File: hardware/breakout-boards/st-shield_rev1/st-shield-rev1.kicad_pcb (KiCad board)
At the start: 4 copper layers, 63.5 x 50.8 mm, 201 parts, among them P1 CONN_01X06, P10 TST, P11 TST, P12 TST, P13 TST, P14 TST, P15 TST, P16 TST, P17 TST, P18 TST, P19 TST, P2 CONN_02X20, P20 TST, P21 TST, P22 TST, P23 TST, P24 TST, P25 TST, P26 TST, P27 TST, P28 TST, P3 CH_A, P4 CH_B, P5 CH_C, P6 PVDD, P7 GND, P8 TST, P9 TST, Q1 Q_PMOS_GSD, Q2 Q_PMOS_GSD, Q3 Q_NMOS_DGS, Q4 Q_NMOS_DGS, Q5 Q_NMOS_DGS, Q6 Q_NMOS_DGS, Q7 Q_NMOS_DGS, Q8 Q_NMOS_DGS, U1 DRV8301_DCA_56, U2 AD8691, U3 AD8691, U4 AD8691, U5 MCP9700-X_TT, U6 MCP9700-X_TT, U7 TLV62565DBVR, U8 AD8691

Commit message: st-shield-rev1: finished board layout. need to clean up (then send to fab)
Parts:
- removed C13, C14, C26, C29, C32: .1u, Capacitors_SMD:C_0603
- removed C15, C42: 100u, Capacitors_SMD:c_elec_6.3x7.7
- removed C16: 10u, Capacitors_SMD:C_2220
- removed C17: .015u, Capacitors_SMD:C_0603
- removed C25, C27, C30: .001u, Capacitors_SMD:C_0603
- removed C28, C31, C33: 100p, Capacitors_SMD:C_0603
- removed C44: 2.2u, Capacitors_SMD:C_0805
- removed C6: 120p, Capacitors_SMD:C_0603
- removed D5: D_Schottky_Small, DO-214AA(SMB):DO-214AA(SMB)
- removed D7: 3.3 Vbkdn, Diodes_SMD:SOD-123
- removed D9: 5Vbkdn, Diodes_SMD:SOD-123
- removed JP1: JUMPER, Pin_Headers:Pin_Header_Straight_1x02
- removed L1: 22u, hackvia:SMD_inductor_5x4mm
- removed L2: 2.2u, hackvia:SMD_inductor_5x4mm
- removed P10, P12, P23, P27, P28: TST, Measurement_Points:Measurement_Point_Round-SMD-Pad_Small
- removed P3: CH_A, Pin_Headers:Pin_Header_Straight_1x01
- removed P4: CH_B, Pin_Headers:Pin_Header_Straight_1x01
- removed P5: CH_C, Pin_Headers:Pin_Header_Straight_1x01
- removed P6: PVDD, Pin_Headers:Pin_Header_Straight_1x01
- removed P7: GND, Pin_Headers:Pin_Header_Straight_1x01
- removed R10: 220k, Resistors_SMD:R_0603
- removed R40: .0003, hackvia:WSL3921
- removed R41, R42, R46, R47, R50, R51: 1k, Resistors_SMD:R_0603
- removed R43, R44, R48, R49, R53, R54: 20k, Resistors_SMD:R_0603
- removed R45, R52, R55: 1.62k, Resistors_SMD:R_0603
- removed R68: 274k, Resistors_SMD:R_0603
- removed R69: 60.4k, Resistors_SMD:R_0603
- removed R7: 118k, Resistors_SMD:R_0603
- removed R71, R72: 82.5k, Resistors_SMD:R_0603
- removed R73: 100, Resistors_SMD:R_0603
- removed R8: 22.1k, Resistors_SMD:R_0603
- removed R9: 16.2k, Resistors_SMD:R_0603
- removed REF** (x23): hack-via, hackvia:hack-via
- removed U1: DRV8301_DCA_56, drv8301:-DCA56_6P35X3P61-M
- removed U2, U3, U4, U8: AD8691, ad8691:-KS_5
- removed U5, U6: MCP9700-X_TT, mcp9700:-SOT-23_MC
- removed U7: TLV62565DBVR, tlv62566:-DBV0005A
- removed W5, W6: NET-TIE, hackvia:nettie
- added MA: hack-via, hackvia:hack-via, F.Cu at (169.9, 116.0)
- added MB: hack-via, hackvia:hack-via, F.Cu at (153.4, 116.1)
- added MC: hack-via, hackvia:hack-via, F.Cu at (136.0, 116.0)
- added U11: DRV8303_DCA_48_SINGLE, DRV8303:drv8303-DCA48_4P42X3P48-M, F.Cu at (151.9, 85.8)
- added V1: hack-via, hackvia:hack-via, F.Cu at (179.6, 102.3)
- added V111111111: hack-via, hackvia:hack-via, F.Cu at (143.8, 81.4)
- added V111111111: hack-via, hackvia:hack-via, F.Cu at (123.8, 78.6)
- added V111111111: hack-via, hackvia:hack-via, F.Cu at (145.3, 78.5)
- added V111111111: hack-via, hackvia:hack-via, F.Cu at (180.8, 122.0)
- added V111111111: hack-via, hackvia:hack-via, F.Cu at (162.1, 119.9)
- added V111111111: hack-via, hackvia:hack-via, F.Cu at (159.9, 121.7)
- added V111111111: hack-via, hackvia:hack-via, F.Cu at (129.5, 120.5)
- added V111111111: hack-via, hackvia:hack-via, F.Cu at (143.3, 116.2)
- added V111111111: hack-via, hackvia:hack-via, F.Cu at (143.3, 117.1)
- added V111111111: hack-via, hackvia:hack-via, F.Cu at (126.5, 110.2)
- added V111111111: hack-via, hackvia:hack-via, F.Cu at (126.1, 109.6)
- added V111111111: hack-via, hackvia:hack-via, F.Cu at (143.8, 82.3)
- added V111111111: hack-via, hackvia:hack-via, F.Cu at (129.3, 116.3)
- added V111111111: hack-via, hackvia:hack-via, F.Cu at (124.7, 117.1)
- added V111111111: hack-via, hackvia:hack-via, F.Cu at (153.5, 75.2)
- added V111111111: hack-via, hackvia:hack-via, F.Cu at (143.8, 77.9)
- added V111111111: hack-via, hackvia:hack-via, F.Cu at (137.2, 76.2)
- added V111111111: hack-via, hackvia:hack-via, F.Cu at (139.7, 76.2)
- added V111111111: hack-via, hackvia:hack-via, F.Cu at (160.4, 95.5)
- added V111111111: hack-via, hackvia:hack-via, F.Cu at (165.9, 95.6)
- added V111111111: hack-via, hackvia:hack-via, F.Cu at (165.9, 92.2)
- added V111111111: hack-via, hackvia:hack-via, F.Cu at (160.5, 92.2)
- added V111111111: hack-via, hackvia:hack-via, F.Cu at (145.3, 82.3)
- added V111111111: hack-via, hackvia:hack-via, F.Cu at (120.9, 97.0)
- added V111111111: hack-via, hackvia:hack-via, F.Cu at (121.0, 104.6)
- added V111111111: hack-via, hackvia:hack-via, F.Cu at (122.3, 114.9)
- added V111111111: hack-via, hackvia:hack-via, F.Cu at (124.8, 122.2)
- added V111111111: hack-via, hackvia:hack-via, F.Cu at (120.9, 118.0)
- added V111111111: hack-via, hackvia:hack-via, F.Cu at (120.9, 122.2)
- added V111111111: hack-via, hackvia:hack-via, F.Cu at (124.8, 69.5)
- added V111111111: hack-via, hackvia:hack-via, F.Cu at (122.8, 69.5)
- added V111111111: hack-via, hackvia:hack-via, F.Cu at (120.5, 69.5)
- added V111111111: hack-via, hackvia:hack-via, F.Cu at (126.6, 80.9)
- added V111111111: hack-via, hackvia:hack-via, F.Cu at (145.3, 81.4)
- added V111111111: hack-via, hackvia:hack-via, F.Cu at (124.1, 83.4)
- added V111111111: hack-via, hackvia:hack-via, F.Cu at (127.6, 88.5)
- added V111111111: hack-via, hackvia:hack-via, F.Cu at (129.0, 88.6)
- added V111111111: hack-via, hackvia:hack-via, F.Cu at (131.6, 92.7)
- added V111111111: hack-via, hackvia:hack-via, F.Cu at (130.2, 95.5)
- added V111111111: hack-via, hackvia:hack-via, F.Cu at (131.1, 95.5)
- added V111111111: hack-via, hackvia:hack-via, F.Cu at (150.1, 84.5)
- added V111111111: hack-via, hackvia:hack-via, F.Cu at (140.0, 81.4)
- added V111111111: hack-via, hackvia:hack-via, F.Cu at (140.3, 82.2)
- added V111111111: hack-via, hackvia:hack-via, F.Cu at (140.3, 83.1)
- added V111111111: hack-via, hackvia:hack-via, F.Cu at (141.4, 83.1)
- added V111111111: hack-via, hackvia:hack-via, F.Cu at (162.1, 117.5)
- added V111111111111: hack-via, hackvia:hack-via, F.Cu at (131.6, 112.9)
- added V1111111111111: hack-via, hackvia:hack-via, F.Cu at (148.8, 112.9)
- added V11111111111111: hack-via, hackvia:hack-via, F.Cu at (165.4, 112.9)
- added V1111111111111111: hack-via, hackvia:hack-via, F.Cu at (175.1, 81.8)
- added V1111111111111112: hack-via, hackvia:hack-via, F.Cu at (175.1, 83.3)
- added V1111111111111113: hack-via, hackvia:hack-via, F.Cu at (175.1, 84.8)
- added V1111111111111114: hack-via, hackvia:hack-via, F.Cu at (175.1, 86.4)
- added V1111111111111115: hack-via, hackvia:hack-via, F.Cu at (175.1, 87.9)
- added V1111111111111116: hack-via, hackvia:hack-via, F.Cu at (175.1, 89.4)
- added V1111111111111121: hack-via, hackvia:hack-via, F.Cu at (176.4, 81.8)
- added V1111111111111122: hack-via, hackvia:hack-via, F.Cu at (176.4, 83.3)
- added V1111111111111123: hack-via, hackvia:hack-via, F.Cu at (176.4, 84.8)
- added V1111111111111124: hack-via, hackvia:hack-via, F.Cu at (176.4, 86.4)
- added V1111111111111125: hack-via, hackvia:hack-via, F.Cu at (176.4, 87.9)
- added V1111111111111126: hack-via, hackvia:hack-via, F.Cu at (176.4, 89.4)
- added V1111111111111131: hack-via, hackvia:hack-via, F.Cu at (177.7, 81.8)
- added V1111111111111132: hack-via, hackvia:hack-via, F.Cu at (177.7, 83.3)
- added V1111111111111133: hack-via, hackvia:hack-via, F.Cu at (177.7, 84.8)
- added V1111111111111134: hack-via, hackvia:hack-via, F.Cu at (177.7, 86.4)
- added V1111111111111135: hack-via, hackvia:hack-via, F.Cu at (177.7, 87.9)
- added V1111111111111136: hack-via, hackvia:hack-via, F.Cu at (177.7, 89.4)
- added V1111111111111141: hack-via, hackvia:hack-via, F.Cu at (178.9, 81.8)
- added V1111111111111142: hack-via, hackvia:hack-via, F.Cu at (178.9, 83.3)
- added V1111111111111143: hack-via, hackvia:hack-via, F.Cu at (178.9, 84.8)
- added V1111111111111144: hack-via, hackvia:hack-via, F.Cu at (178.9, 86.4)
- added V1111111111111145: hack-via, hackvia:hack-via, F.Cu at (178.9, 87.9)
- added V1111111111111146: hack-via, hackvia:hack-via, F.Cu at (178.9, 89.4)
- added V1111111111111151: hack-via, hackvia:hack-via, F.Cu at (180.2, 81.8)
- added V1111111111111152: hack-via, hackvia:hack-via, F.Cu at (180.2, 83.3)
- added V1111111111111153: hack-via, hackvia:hack-via, F.Cu at (180.2, 84.8)
- added V1111111111111154: hack-via, hackvia:hack-via, F.Cu at (180.2, 86.4)
- added V1111111111111155: hack-via, hackvia:hack-via, F.Cu at (180.2, 87.9)
- added V1111111111111156: hack-via, hackvia:hack-via, F.Cu at (180.2, 89.4)
- added V1111111111111161: hack-via, hackvia:hack-via, F.Cu at (181.5, 81.8)
- added V1111111111111162: hack-via, hackvia:hack-via, F.Cu at (181.5, 83.3)
- added V1111111111111163: hack-via, hackvia:hack-via, F.Cu at (181.5, 84.8)
- added V1111111111111164: hack-via, hackvia:hack-via, F.Cu at (181.5, 86.4)
- added V1111111111111165: hack-via, hackvia:hack-via, F.Cu at (181.5, 87.9)
- added V1111111111111166: hack-via, hackvia:hack-via, F.Cu at (181.5, 89.4)
- added V11111111111112: hack-via, hackvia:hack-via, F.Cu at (165.4, 114.2)
- added V11111111111113: hack-via, hackvia:hack-via, F.Cu at (165.4, 115.4)
- added V11111111111114: hack-via, hackvia:hack-via, F.Cu at (165.4, 116.7)
- added V11111111111115: hack-via, hackvia:hack-via, F.Cu at (165.4, 118.0)
- added V11111111111116: hack-via, hackvia:hack-via, F.Cu at (165.4, 119.3)
- added V1111111111112: hack-via, hackvia:hack-via, F.Cu at (148.8, 114.2)
- added V11111111111121: hack-via, hackvia:hack-via, F.Cu at (166.9, 112.9)
- added V11111111111122: hack-via, hackvia:hack-via, F.Cu at (166.9, 114.2)
- added V11111111111123: hack-via, hackvia:hack-via, F.Cu at (166.9, 115.4)
- added V11111111111124: hack-via, hackvia:hack-via, F.Cu at (166.9, 116.7)
- added V11111111111125: hack-via, hackvia:hack-via, F.Cu at (166.9, 118.0)
- added V11111111111126: hack-via, hackvia:hack-via, F.Cu at (166.9, 119.3)
- added V1111111111113: hack-via, hackvia:hack-via, F.Cu at (148.8, 115.4)
- added V11111111111131: hack-via, hackvia:hack-via, F.Cu at (168.4, 112.9)
- added V11111111111132: hack-via, hackvia:hack-via, F.Cu at (168.4, 114.2)
- added V11111111111133: hack-via, hackvia:hack-via, F.Cu at (168.4, 115.4)
- added V11111111111134: hack-via, hackvia:hack-via, F.Cu at (168.4, 116.7)
- added V11111111111135: hack-via, hackvia:hack-via, F.Cu at (168.4, 118.0)
- added V11111111111136: hack-via, hackvia:hack-via, F.Cu at (168.4, 119.3)
- added V1111111111114: hack-via, hackvia:hack-via, F.Cu at (148.8, 116.7)
- added V11111111111141: hack-via, hackvia:hack-via, F.Cu at (169.9, 112.9)
- added V11111111111142: hack-via, hackvia:hack-via, F.Cu at (169.9, 114.2)
- added V11111111111143: hack-via, hackvia:hack-via, F.Cu at (169.9, 115.4)
- added V11111111111144: hack-via, hackvia:hack-via, F.Cu at (169.9, 116.7)
- added V11111111111145: hack-via, hackvia:hack-via, F.Cu at (169.9, 118.0)
- added V11111111111146: hack-via, hackvia:hack-via, F.Cu at (169.9, 119.3)
- added V1111111111115: hack-via, hackvia:hack-via, F.Cu at (148.8, 118.0)
- added V11111111111151: hack-via, hackvia:hack-via, F.Cu at (171.4, 112.9)
- added V11111111111152: hack-via, hackvia:hack-via, F.Cu at (171.4, 114.2)
- added V11111111111153: hack-via, hackvia:hack-via, F.Cu at (171.4, 115.4)
- added V11111111111154: hack-via, hackvia:hack-via, F.Cu at (171.4, 116.7)
- added V11111111111155: hack-via, hackvia:hack-via, F.Cu at (171.4, 118.0)
- added V11111111111156: hack-via, hackvia:hack-via, F.Cu at (171.4, 119.3)
- added V1111111111116: hack-via, hackvia:hack-via, F.Cu at (148.8, 119.3)
- added V11111111111161: hack-via, hackvia:hack-via, F.Cu at (173.0, 112.9)
- added V11111111111162: hack-via, hackvia:hack-via, F.Cu at (173.0, 114.2)
- added V11111111111163: hack-via, hackvia:hack-via, F.Cu at (173.0, 115.4)
- added V11111111111164: hack-via, hackvia:hack-via, F.Cu at (173.0, 116.7)
- added V11111111111165: hack-via, hackvia:hack-via, F.Cu at (173.0, 118.0)
- added V11111111111166: hack-via, hackvia:hack-via, F.Cu at (173.0, 119.3)
- added V11111111111171: hack-via, hackvia:hack-via, F.Cu at (174.5, 112.9)
- added V11111111111172: hack-via, hackvia:hack-via, F.Cu at (174.5, 114.2)
- added V11111111111173: hack-via, hackvia:hack-via, F.Cu at (174.5, 115.4)
- added V11111111111174: hack-via, hackvia:hack-via, F.Cu at (174.5, 116.7)
- added V11111111111175: hack-via, hackvia:hack-via, F.Cu at (174.5, 118.0)
- added V11111111111176: hack-via, hackvia:hack-via, F.Cu at (174.5, 119.3)
- added V111111111112: hack-via, hackvia:hack-via, F.Cu at (131.6, 114.2)
- added V1111111111121: hack-via, hackvia:hack-via, F.Cu at (150.4, 112.9)
- added V1111111111122: hack-via, hackvia:hack-via, F.Cu at (150.4, 114.2)
- added V1111111111123: hack-via, hackvia:hack-via, F.Cu at (150.4, 115.4)
- added V1111111111124: hack-via, hackvia:hack-via, F.Cu at (150.4, 116.7)
- added V1111111111125: hack-via, hackvia:hack-via, F.Cu at (150.4, 118.0)
- added V1111111111126: hack-via, hackvia:hack-via, F.Cu at (150.4, 119.3)
- added V111111111113: hack-via, hackvia:hack-via, F.Cu at (131.6, 115.4)
- added V1111111111131: hack-via, hackvia:hack-via, F.Cu at (151.9, 112.9)
- added V1111111111132: hack-via, hackvia:hack-via, F.Cu at (151.9, 114.2)
- added V1111111111133: hack-via, hackvia:hack-via, F.Cu at (151.9, 115.4)
- added V1111111111134: hack-via, hackvia:hack-via, F.Cu at (151.9, 116.7)
- added V1111111111135: hack-via, hackvia:hack-via, F.Cu at (151.9, 118.0)
- added V1111111111136: hack-via, hackvia:hack-via, F.Cu at (151.9, 119.3)
- added V111111111114: hack-via, hackvia:hack-via, F.Cu at (131.6, 116.7)
- added V1111111111141: hack-via, hackvia:hack-via, F.Cu at (153.4, 112.9)
- added V1111111111142: hack-via, hackvia:hack-via, F.Cu at (153.4, 114.2)
- added V1111111111143: hack-via, hackvia:hack-via, F.Cu at (153.4, 115.4)
- added V1111111111144: hack-via, hackvia:hack-via, F.Cu at (153.4, 116.7)
- added V1111111111145: hack-via, hackvia:hack-via, F.Cu at (153.4, 118.0)
- added V1111111111146: hack-via, hackvia:hack-via, F.Cu at (153.4, 119.3)
- added V111111111115: hack-via, hackvia:hack-via, F.Cu at (131.6, 118.0)
- added V1111111111151: hack-via, hackvia:hack-via, F.Cu at (154.9, 112.9)
- added V1111111111152: hack-via, hackvia:hack-via, F.Cu at (154.9, 114.2)
- added V1111111111153: hack-via, hackvia:hack-via, F.Cu at (154.9, 115.4)
- added V1111111111154: hack-via, hackvia:hack-via, F.Cu at (154.9, 116.7)
- added V1111111111155: hack-via, hackvia:hack-via, F.Cu at (154.9, 118.0)
- added V1111111111156: hack-via, hackvia:hack-via, F.Cu at (154.9, 119.3)
- added V111111111116: hack-via, hackvia:hack-via, F.Cu at (131.6, 119.3)
- added V1111111111161: hack-via, hackvia:hack-via, F.Cu at (156.5, 112.9)
- added V1111111111162: hack-via, hackvia:hack-via, F.Cu at (156.5, 114.2)
- added V1111111111163: hack-via, hackvia:hack-via, F.Cu at (156.5, 115.4)
- added V1111111111164: hack-via, hackvia:hack-via, F.Cu at (156.5, 116.7)
- added V1111111111165: hack-via, hackvia:hack-via, F.Cu at (156.5, 118.0)
- added V1111111111166: hack-via, hackvia:hack-via, F.Cu at (156.5, 119.3)
- added V1111111111171: hack-via, hackvia:hack-via, F.Cu at (158.0, 112.9)
- added V1111111111172: hack-via, hackvia:hack-via, F.Cu at (158.0, 114.2)
- added V1111111111173: hack-via, hackvia:hack-via, F.Cu at (158.0, 115.4)
- added V1111111111174: hack-via, hackvia:hack-via, F.Cu at (158.0, 116.7)
- added V1111111111175: hack-via, hackvia:hack-via, F.Cu at (158.0, 118.0)
- added V1111111111176: hack-via, hackvia:hack-via, F.Cu at (158.0, 119.3)
- added V111111111121: hack-via, hackvia:hack-via, F.Cu at (133.1, 112.9)
- added V111111111122: hack-via, hackvia:hack-via, F.Cu at (133.1, 114.2)
- added V111111111123: hack-via, hackvia:hack-via, F.Cu at (133.1, 115.4)
- added V111111111124: hack-via, hackvia:hack-via, F.Cu at (133.1, 116.7)
- added V111111111125: hack-via, hackvia:hack-via, F.Cu at (133.1, 118.0)
- added V111111111126: hack-via, hackvia:hack-via, F.Cu at (133.1, 119.3)
- added V111111111131: hack-via, hackvia:hack-via, F.Cu at (134.6, 112.9)
- added V111111111132: hack-via, hackvia:hack-via, F.Cu at (134.6, 114.2)
- added V111111111133: hack-via, hackvia:hack-via, F.Cu at (134.6, 115.4)
- added V111111111134: hack-via, hackvia:hack-via, F.Cu at (134.6, 116.7)
- added V111111111135: hack-via, hackvia:hack-via, F.Cu at (134.6, 118.0)
- added V111111111136: hack-via, hackvia:hack-via, F.Cu at (134.6, 119.3)
- added V111111111141: hack-via, hackvia:hack-via, F.Cu at (136.1, 112.9)
- added V111111111142: hack-via, hackvia:hack-via, F.Cu at (136.1, 114.2)
- added V111111111143: hack-via, hackvia:hack-via, F.Cu at (136.1, 115.4)
- added V111111111144: hack-via, hackvia:hack-via, F.Cu at (136.1, 116.7)
- added V111111111145: hack-via, hackvia:hack-via, F.Cu at (136.1, 118.0)
- added V111111111146: hack-via, hackvia:hack-via, F.Cu at (136.1, 119.3)
- added V111111111151: hack-via, hackvia:hack-via, F.Cu at (137.7, 112.9)
- added V111111111152: hack-via, hackvia:hack-via, F.Cu at (137.7, 114.2)
- added V111111111153: hack-via, hackvia:hack-via, F.Cu at (137.7, 115.4)
- added V111111111154: hack-via, hackvia:hack-via, F.Cu at (137.7, 116.7)
- added V111111111155: hack-via, hackvia:hack-via, F.Cu at (137.7, 118.0)
- added V111111111156: hack-via, hackvia:hack-via, F.Cu at (137.7, 119.3)
- added V111111111161: hack-via, hackvia:hack-via, F.Cu at (139.2, 112.9)
- added V111111111162: hack-via, hackvia:hack-via, F.Cu at (139.2, 114.2)
- added V111111111163: hack-via, hackvia:hack-via, F.Cu at (139.2, 115.4)
- added V111111111164: hack-via, hackvia:hack-via, F.Cu at (139.2, 116.7)
- added V111111111165: hack-via, hackvia:hack-via, F.Cu at (139.2, 118.0)
- added V111111111166: hack-via, hackvia:hack-via, F.Cu at (139.2, 119.3)
- added V111111111171: hack-via, hackvia:hack-via, F.Cu at (140.7, 112.9)
- added V111111111172: hack-via, hackvia:hack-via, F.Cu at (140.7, 114.2)
- added V111111111173: hack-via, hackvia:hack-via, F.Cu at (140.7, 115.4)
- added V111111111174: hack-via, hackvia:hack-via, F.Cu at (140.7, 116.7)
- added V111111111175: hack-via, hackvia:hack-via, F.Cu at (140.7, 118.0)
- added V111111111176: hack-via, hackvia:hack-via, F.Cu at (140.7, 119.3)
- added V111111112: hack-via, hackvia:hack-via, F.Cu at (150.1, 85.1)
- added V111111113: hack-via, hackvia:hack-via, F.Cu at (150.1, 85.7)
- added V111111114: hack-via, hackvia:hack-via, F.Cu at (150.1, 86.4)
- added V111111115: hack-via, hackvia:hack-via, F.Cu at (150.1, 87.0)
- added V111111121: hack-via, hackvia:hack-via, F.Cu at (151.0, 84.5)
- added V111111122: hack-via, hackvia:hack-via, F.Cu at (151.0, 85.1)
- added V111111123: hack-via, hackvia:hack-via, F.Cu at (151.0, 85.7)
- added V111111124: hack-via, hackvia:hack-via, F.Cu at (151.0, 86.4)
- added V111111125: hack-via, hackvia:hack-via, F.Cu at (151.0, 87.0)
- added V111111131: hack-via, hackvia:hack-via, F.Cu at (151.9, 84.5)
- added V111111132: hack-via, hackvia:hack-via, F.Cu at (151.9, 85.1)
- added V111111133: hack-via, hackvia:hack-via, F.Cu at (151.9, 85.7)
- added V111111134: hack-via, hackvia:hack-via, F.Cu at (151.9, 86.4)
- added V111111135: hack-via, hackvia:hack-via, F.Cu at (151.9, 87.0)
- added V111111141: hack-via, hackvia:hack-via, F.Cu at (152.8, 84.5)
- added V111111142: hack-via, hackvia:hack-via, F.Cu at (152.8, 85.1)
- added V111111143: hack-via, hackvia:hack-via, F.Cu at (152.8, 85.7)
- added V111111144: hack-via, hackvia:hack-via, F.Cu at (152.8, 86.4)
- added V111111145: hack-via, hackvia:hack-via, F.Cu at (152.8, 87.0)
- added V111111151: hack-via, hackvia:hack-via, F.Cu at (153.7, 84.5)
- added V111111152: hack-via, hackvia:hack-via, F.Cu at (153.7, 85.1)
- added V111111153: hack-via, hackvia:hack-via, F.Cu at (153.7, 85.7)
- added V111111154: hack-via, hackvia:hack-via, F.Cu at (153.7, 86.4)
- added V111111155: hack-via, hackvia:hack-via, F.Cu at (153.7, 87.0)
- added V2: hack-via, hackvia:hack-via, F.Cu at (126.2, 101.7)
- added V3: hack-via, hackvia:hack-via, F.Cu at (134.5, 85.3)
- added V4: hack-via, hackvia:hack-via, F.Cu at (178.2, 85.4)
- C18, C20, C21, C23, R14, R15, R19, R20, R21, R23, R24, R31, R34, R35, R39: moved to B.Cu
- C4: value .1u -> 1000p; moved to B.Cu
- C5: value 6800p -> 1000p; moved to B.Cu
- C9: value 10u -> 4.7u
- R1, R2, R3, R4: footprint Resistors_SMD:R_0805 -> Resistors_SMD:R_0603
- moved R59 251.9 mm to (124.2, 91.3), turned to 270 degrees
- moved R60 251.3 mm to (124.2, 94.2), turned to 270 degrees
- moved R58 247.5 mm to (124.2, 88.5), turned to 270 degrees
- moved R61 245.9 mm to (126.4, 88.5), turned to 270 degrees
- moved R63 241.0 mm to (126.4, 94.2), turned to 270 degrees
- moved C36 240.2 mm to (128.3, 91.6), turned to 270 degrees
- moved R62 237.0 mm to (126.4, 91.3), turned to 270 degrees
- moved C35 235.6 mm to (128.3, 88.5), turned to 270 degrees
- moved C37 229.7 mm to (128.3, 94.7), turned to 270 degrees
- moved P26 227.8 mm to (130.5, 94.0)
- moved R65 224.4 mm to (130.8, 81.0)
- moved R66 221.8 mm to (137.9, 82.4), turned to 180 degrees
- moved P24 221.5 mm to (130.5, 88.8)
- moved P25 221.1 mm to (130.4, 91.6)
- moved R64 211.8 mm to (138.0, 88.0), turned to 270 degrees
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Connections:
- C4 pad 1: 3V3 -> /MOSFET Array/CUR_CP
- C4 pad 2: GND -> /MOSFET Array/CUR_CN
- C5 pad 1: Net-(C5-Pad1) -> /MOSFET Array/CUR_BP
- C5 pad 2: GND -> /MOSFET Array/CUR_BN
- P2 pad 1: Net-(JP1-Pad2) -> 3V3
- P2 pad 16: /Temperature Sensors/T1 -> /FET Driver/SO1
- P2 pad 18: /Temperature Sensors/T2 -> /FET Driver/SO2
- P2 pad 20: Net-(P2-Pad20) -> (no net)
- P2 pad 22: /Shunt Amplifiers/IA -> /Hall Effect Sensor Filters/HALL_A_OUT
- P2 pad 24: /Shunt Amplifiers/IB -> /Hall Effect Sensor Filters/HALL_B_OUT
- P2 pad 26: /Shunt Amplifiers/IC -> (no net)
- P2 pad 28: /Hall Effect Sensor Filters/HALL_A_OUT -> /Power Management/DC_IN
- P2 pad 3: Net-(JP1-Pad2) -> 5V
- P2 pad 30: /Hall Effect Sensor Filters/HALL_B_OUT -> GND
- P2 pad 32: /Hall Effect Sensor Filters/HALL_C_OUT -> GND
- P2 pad 34: /Power Management/DC_IN -> GND
- P20 pad 1: Net-(P20-Pad1) -> (no net)
- Q4 pad 3: /FET Driver/SL_A -> GND
- R22 pad 2: /FET Driver/SL_A -> /FET Driver/SL_C
- W1 pad 1: /FET Driver/SL_A -> /FET Driver/SL_C
- W1 pad 2: /MOSFET Array/CUR_AP -> /MOSFET Array/CUR_CP
- W2 pad 2: /MOSFET Array/CUR_AN -> /MOSFET Array/CUR_CN
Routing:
- net /MOSFET Array/AEMF: track 0.00 -> 116.0 mm, vias 0 -> 2
- net 3V3: track 1.27 -> 115.2 mm, vias 0 -> 1
- net /MOSFET Array/BEMF: track 0.00 -> 100.6 mm, vias 0 -> 1
- net GND: track 1.50 -> 90.1 mm, vias 0 -> 2
- net /Hall Effect Sensor Filters/HALL_A_OUT: track 0.00 -> 77.6 mm, vias 0 -> 2
- net /MOSFET Array/MOTOR_N: track 0.00 -> 72.3 mm, vias 0 -> 4
- net /MOSFET Array/CEMF: track 0.00 -> 65.6 mm, vias 0 -> 1
- net Net-(R27-Pad1): track 0.00 -> 64.3 mm
- net /Power Management/DC_IN: track 0.00 -> 51.5 mm
- net /Hall Effect Sensor Filters/HALL_B_OUT: track 0.00 -> 47.1 mm, vias 0 -> 1
- net /Temperature Sensors/T0: track 0.00 -> 30.2 mm
- net /MOSFET Array/MOTOR_A: track 3.22 -> 32.1 mm, vias 0 -> 2
- net /MOSFET Array/A_HI: track 0.00 -> 27.5 mm, vias 0 -> 2
- net /FET Driver/SO2: track 0.00 -> 26.9 mm, vias 0 -> 1
- net /FET Driver/FAULT: track 0.00 -> 23.2 mm
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- added copper zone on F.Cu, net GND
- removed copper zone on B.Cu, net /FET Driver/SL_A
- removed copper zone on In2.Cu, net GND
- removed copper zone on In1.Cu, net PVDD
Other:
- board size 63.5 x 50.8 mm -> 63.5 x 55.4 mm
- copper layers 4 -> 2
- board text added: "A"
- board text added: "B"
- board text added: "C"
- board text added: "DEBUG"
- board text added: "FAULT"
- board text added: "G N D"
- board text added: "OCTW"
- board text added: "P V D D"
- board text added: "PWR"

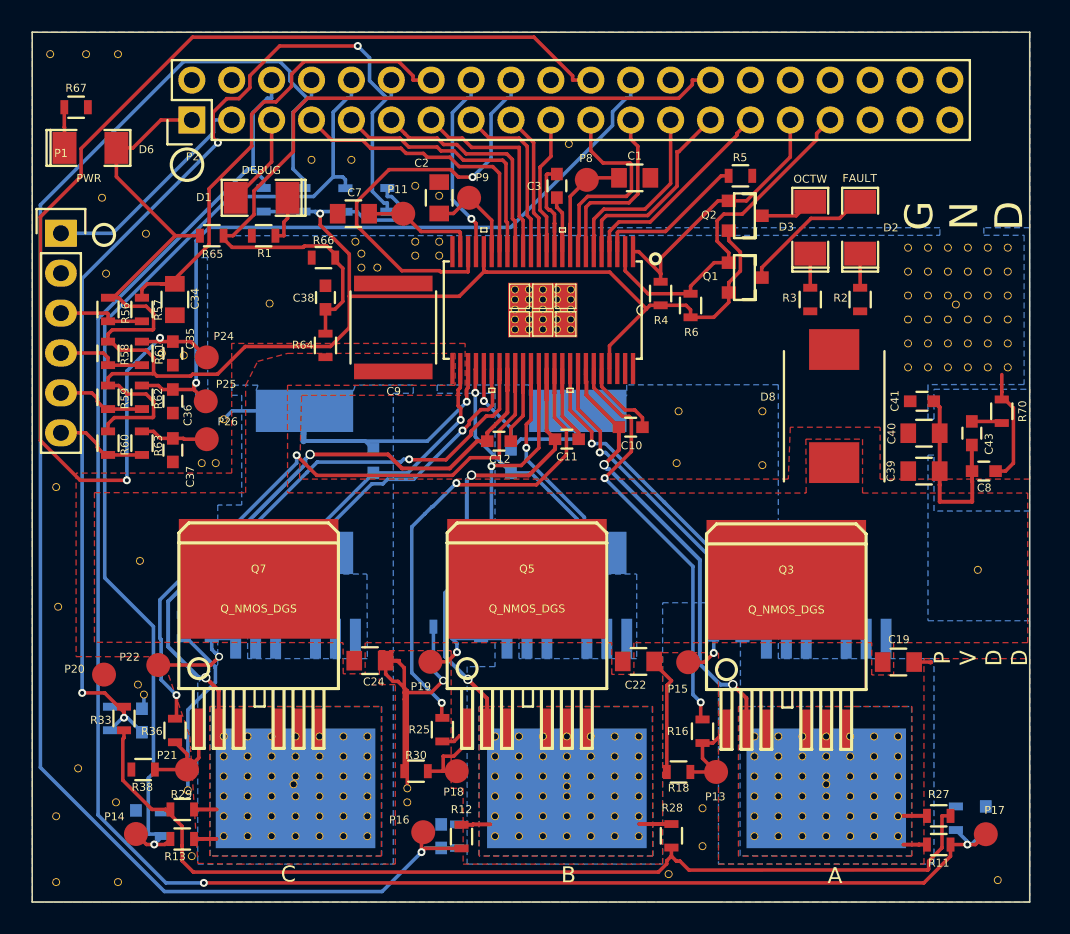
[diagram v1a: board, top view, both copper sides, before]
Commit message: shield rev1: finalized routing, mounting holes, and silk screen refs. need to add logo
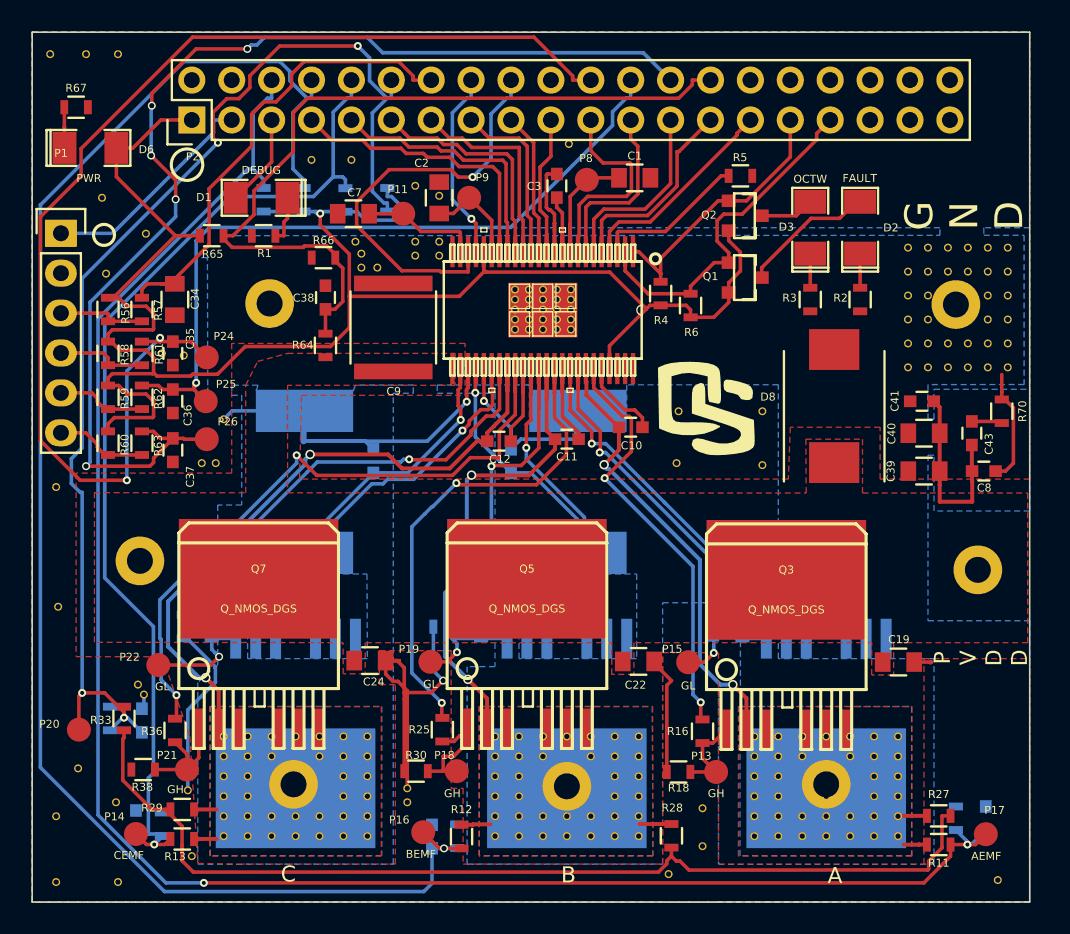
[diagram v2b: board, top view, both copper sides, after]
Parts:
- removed V1111111111111133, V1111111111111134, V1111111111111143, V1111111111111144, V11111111111133, V11111111111134, V11111111111142, V11111111111153, V11111111111154, V1111111111133, V1111111111134, V1111111111142, V1111111111143, V1111111111144, V1111111111153, V1111111111154, V111111111133, V111111111134, V111111111142, V111111111143, V111111111144, V111111111153, V111111111154: hack-via, hackvia:hack-via
- added G***: LOGO, hackvia:LOGO, F.Cu at (162.2, 91.9)
- moved P20 3.85 mm to (122.4, 112.5)
- moved C20 0.58 mm to (144.8, 119.3)
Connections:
- P2 pad 20: (no net) -> Net-(P2-Pad20)
- P2 pad 26: (no net) -> /Hall Effect Sensor Filters/HALL_C_OUT
- P20 pad 1: (no net) -> /MOSFET Array/MOTOR_N
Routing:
- net /Hall Effect Sensor Filters/HALL_C_OUT: track 4.33 -> 73.2 mm, vias 0 -> 5
- net /MOSFET Array/MOTOR_N: track 72.3 -> 75.4 mm
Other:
- rule via_min_size: 0.381 -> 0.508
- board text added: "AEMF"
- board text added: "BEMF"
- board text added: "CEMF"
- board text added: "GH"
- board text added: "GL"

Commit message: st-shield-rev1: sent to fab
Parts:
- moved G*** 1.47 mm to (162.2, 90.5)
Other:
- board text added: "ASME"
- board text added: "Brian Bove 2015"
- board text added: "SEM"
